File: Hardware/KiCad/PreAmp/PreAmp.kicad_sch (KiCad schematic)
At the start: 27 parts, among them J1 XLR3, J2 Conn_01x03_Pin, J3 Conn_01x05_Pin, U1 TLV2371DBV, U2 INA217AIDWR

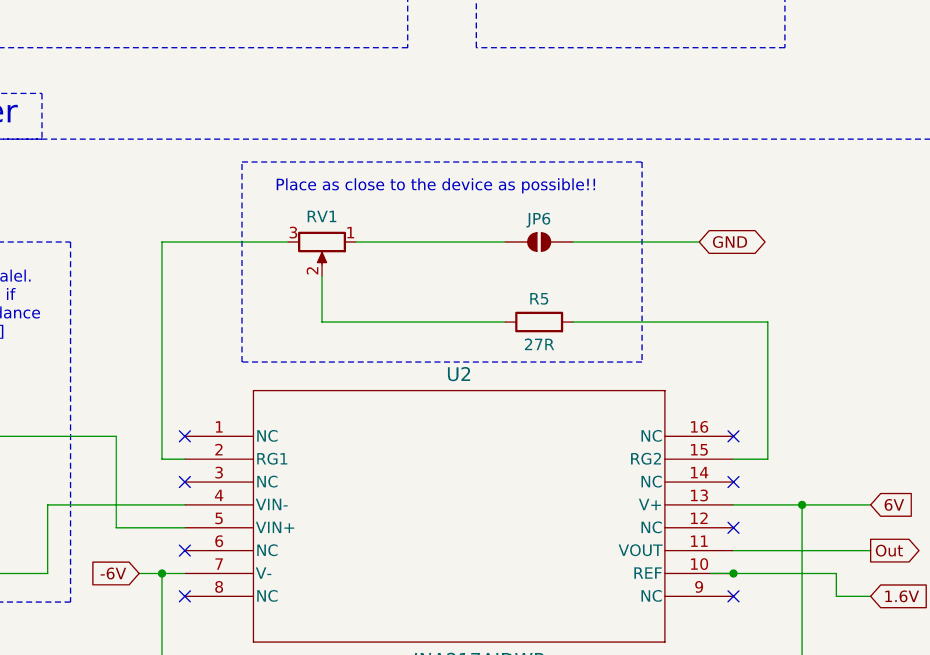
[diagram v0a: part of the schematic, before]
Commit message: Changed flow -> right to left
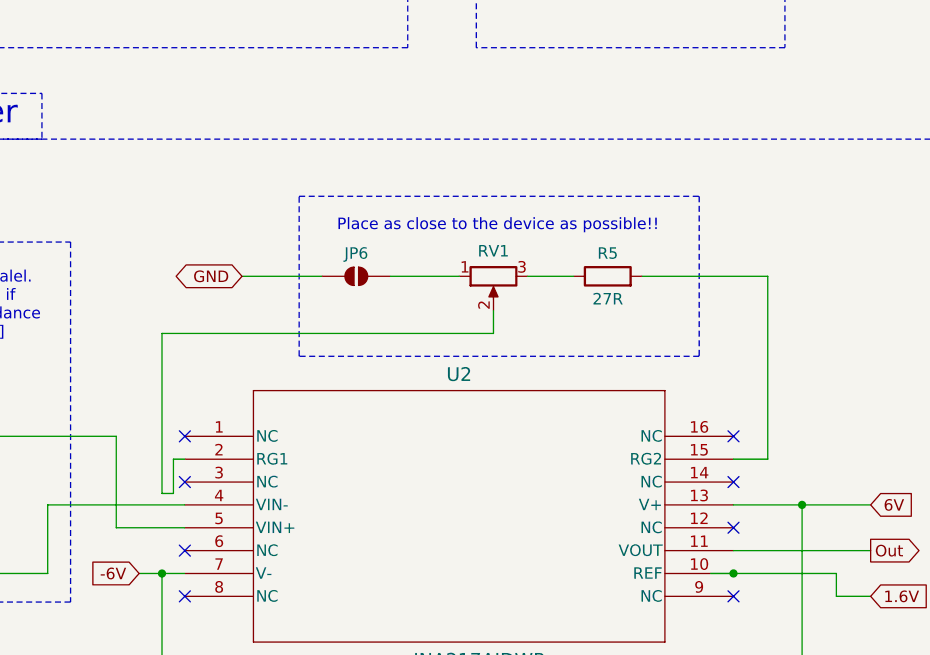
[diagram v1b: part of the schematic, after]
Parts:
- J2: footprint (none) -> Connector_PinSocket_2.54mm:PinSocket_1x03_P2.54mm_Vertical
- R1, R2, R3, R4, R5: footprint (none) -> Capacitor_SMD:C_0805_2012Metric
- TP1, TP2, TP3: footprint TestPoint:TestPoint_Pad_D3.0mm -> TestPoint:TestPoint_Pad_D2.0mm
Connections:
- net at RV1.2: now also U2.2 (RG1); no longer R5.1
- net at RV1.3: now also R5.1; no longer U2.2 (RG1)
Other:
- moved on the sheet: JP6, R5, RV1
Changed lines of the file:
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@@
 	)
 	(rectangle
-		(start 180.34 64.77)
-		(end 224.79 86.995)
+		(start 186.69 68.58)
+		(end 231.14 86.36)
 		(stroke
 			(width 0)
@@
 	(text "Place as close to the device as possible!!"
 		(exclude_from_sim no)
-		(at 201.93 67.564 0)
+		(at 208.788 71.882 0)
 		(effects
 			(font
@@
 	(wire
 		(pts
-			(xy 171.45 73.66) (xy 171.45 97.79)
-		)
-		(stroke
-			(width 0)
-			(type default)
-		)
-	)
-	(wire
-		(pts
 			(xy 170.18 41.91) (xy 163.83 41.91)
 		)
@@
 	(wire
 		(pts
-			(xy 238.76 82.55) (xy 238.76 97.79)
+			(xy 171.45 83.82) (xy 171.45 101.6)
 		)
 		(stroke
@@
 	(wire
 		(pts
+			(xy 217.17 77.47) (xy 212.09 77.47)
+		)
+		(stroke
+			(width 0)
+			(type default)
+		)
+	)
+	(wire
+		(pts
 			(xy 120.65 110.49) (xy 120.65 118.11)
 		)
@@
 	(wire
 		(pts
-			(xy 173.99 97.79) (xy 171.45 97.79)
+			(xy 171.45 83.82) (xy 208.28 83.82)
+		)
+		(stroke
+			(width 0)
+			(type default)
+		)
+	)
+	(wire
+		(pts
+			(xy 172.72 101.6) (xy 171.45 101.6)
 		)
 		(stroke
@@
 	(wire
 		(pts
-			(xy 189.23 77.47) (xy 189.23 82.55)
-		)
-		(stroke
-			(width 0)
-			(type default)
-		)
-	)
-	(wire
-		(pts
 			(xy 217.17 30.48) (xy 229.87 30.48)
 		)
@@
 	(wire
 		(pts
-			(xy 171.45 73.66) (xy 185.42 73.66)
+			(xy 172.72 97.79) (xy 173.99 97.79)
 		)
 		(stroke
@@
 	(wire
 		(pts
+			(xy 234.95 97.79) (xy 238.76 97.79)
+		)
+		(stroke
+			(width 0)
+			(type default)
+		)
+	)
+	(wire
+		(pts
 			(xy 72.39 41.91) (xy 72.39 46.99)
 		)
@@
 	(wire
 		(pts
-			(xy 118.11 45.72) (xy 124.46 45.72)
+			(xy 238.76 77.47) (xy 238.76 97.79)
 		)
 		(stroke
@@
 	(wire
 		(pts
-			(xy 234.95 97.79) (xy 238.76 97.79)
+			(xy 118.11 45.72) (xy 124.46 45.72)
 		)
 		(stroke
@@
 	(wire
 		(pts
-			(xy 217.17 82.55) (xy 238.76 82.55)
+			(xy 172.72 38.1) (xy 172.72 43.18)
 		)
 		(stroke
@@
 	(wire
 		(pts
-			(xy 172.72 38.1) (xy 172.72 43.18)
+			(xy 246.38 113.03) (xy 246.38 110.49)
 		)
 		(stroke
@@
 	(wire
 		(pts
-			(xy 246.38 113.03) (xy 246.38 110.49)
+			(xy 125.73 40.64) (xy 125.73 35.56)
 		)
 		(stroke
@@
 	(wire
 		(pts
-			(xy 125.73 40.64) (xy 125.73 35.56)
+			(xy 172.72 101.6) (xy 172.72 97.79)
 		)
 		(stroke
@@
 	(wire
 		(pts
-			(xy 193.04 73.66) (xy 209.55 73.66)
+			(xy 204.47 77.47) (xy 196.85 77.47)
 		)
 		(stroke
@@
 	(wire
 		(pts
-			(xy 189.23 82.55) (xy 209.55 82.55)
-		)
-		(stroke
-			(width 0)
-			(type default)
-		)
-	)
-	(wire
-		(pts
 			(xy 83.82 161.29) (xy 102.87 161.29)
 		)
@@
 	(wire
 		(pts
-			(xy 217.17 73.66) (xy 231.14 73.66)
+			(xy 189.23 77.47) (xy 180.34 77.47)
 		)
 		(stroke
@@
 	(wire
 		(pts
+			(xy 208.28 83.82) (xy 208.28 81.28)
+		)
+		(stroke
+			(width 0)
+			(type default)
+		)
+	)
+	(wire
+		(pts
 			(xy 90.17 80.01) (xy 106.68 80.01)
 		)
@@
 	(wire
 		(pts
+			(xy 238.76 77.47) (xy 224.79 77.47)
+		)
+		(stroke
+			(width 0)
+			(type default)
+		)
+	)
+	(wire
+		(pts
 			(xy 102.87 161.29) (xy 102.87 170.18)
 		)
@@
 	(global_label "GND"
 		(shape bidirectional)
-		(at 231.14 73.66 0)
+		(at 180.34 77.47 180)
 		(fields_autoplaced yes)
 		(effects
@@
 				(size 1.27 1.27)
 			)
-			(justify left)
+			(justify right)
 		)
 		(property "Intersheetrefs" "${INTERSHEET_REFS}"
-			(at 239.107 73.66 0)
+			(at 172.373 77.47 0)
 			(effects
 				(font
 					(size 1.27 1.27)
 				)
-				(justify left)
+				(justify right)
 				(hide yes)
 			)
@@
 			)
 		)
-		(property "Footprint" ""
+		(property "Footprint" "Capacitor_SMD:C_0805_2012Metric"
 			(at 68.072 163.83 90)
 			(effects
@@
 	(symbol
 		(lib_id "Device:R_Potentiometer")
-		(at 189.23 73.66 270)
+		(at 208.28 77.47 90)
+		(mirror x)
 		(unit 1)
 		(exclude_from_sim no)
@@
 		(dnp no)
 		(property "Reference" "RV1"
-			(at 189.23 70.866 90)
+			(at 208.28 74.676 90)
 			(effects
 				(font
@@
 		)
 		(property "Value" "R_Potentiometer"
-			(at 189.484 70.358 90)
+			(at 208.026 74.168 90)
 			(effects
 				(font
@@
 		)
 		(property "Footprint" "Potentiometer_THT:Potentiometer_Alpha_RD901F-40-00D_Single_Vertical"
-			(at 189.23 73.66 0)
+			(at 208.28 77.47 0)
 			(effects
 				(font
@@
 		)
 		(property "Datasheet" "~"
-			(at 189.23 73.66 0)
+			(at 208.28 77.47 0)
 			(effects
 				(font
@@
 		)
 		(property "Description" "Potentiometer"
-			(at 189.23 73.66 0)
+			(at 208.28 77.47 0)
 			(effects
 				(font
@@
 			)
 		)
-		(property "Footprint" ""
+		(property "Footprint" "Capacitor_SMD:C_0805_2012Metric"
 			(at 127.762 121.92 90)
 			(effects
@@
 			)
 		)
-		(property "Footprint" ""
+		(property "Footprint" "Connector_PinSocket_2.54mm:PinSocket_1x03_P2.54mm_Vertical"
 			(at 135.89 38.1 0)
 			(effects
@@
 			)
 		)
-		(property "Footprint" "TestPoint:TestPoint_Pad_D3.0mm"
+		(property "Footprint" "TestPoint:TestPoint_Pad_D2.0mm"
 			(at 115.57 170.18 0)
 			(effects
@@
 			)
 		)
-		(property "Footprint" "TestPoint:TestPoint_Pad_D3.0mm"
+		(property "Footprint" "TestPoint:TestPoint_Pad_D2.0mm"
 			(at 152.4 133.35 0)
 			(effects
@@
 			)
 		)
-		(property "Footprint" "TestPoint:TestPoint_Pad_D3.0mm"
+		(property "Footprint" "TestPoint:TestPoint_Pad_D2.0mm"
 			(at 123.19 45.72 0)
 			(effects
@@
 	(symbol
 		(lib_id "Device:R")
-		(at 213.36 82.55 90)
+		(at 220.98 77.47 90)
 		(unit 1)
 		(exclude_from_sim no)
@@
 		(dnp no)
 		(property "Reference" "R5"
-			(at 213.36 80.01 90)
+			(at 220.98 74.93 90)
 			(effects
 				(font
@@
 		)
 		(property "Value" "27R"
-			(at 213.36 85.09 90)
+			(at 220.98 80.01 90)
 			(effects
 				(font
@@
 			)
 		)
-		(property "Footprint" ""
-			(at 213.36 84.328 90)
+		(property "Footprint" "Capacitor_SMD:C_0805_2012Metric"
+			(at 220.98 79.248 90)
 			(effects
 				(font
@@
 		)
 		(property "Datasheet" "~"
-			(at 213.36 82.55 0)
+			(at 220.98 77.47 0)
 			(effects
 				(font
@@
 		)
 		(property "Description" "Resistor"
-			(at 213.36 82.55 0)
+			(at 220.98 77.47 0)
 			(effects
 				(font
@@
 			)
 		)
-		(property "Footprint" ""
+		(property "Footprint" "Capacitor_SMD:C_0805_2012Metric"
 			(at 68.072 180.34 90)
 			(effects
@@
 			)
 		)
-		(property "Footprint" ""
+		(property "Footprint" "Capacitor_SMD:C_0805_2012Metric"
 			(at 118.872 121.92 90)
 			(effects
@@
 	(symbol
 		(lib_id "Jumper:SolderJumper_2_Open")
-		(at 213.36 73.66 0)
+		(at 193.04 77.47 0)
+		(mirror y)
 		(unit 1)
 		(exclude_from_sim no)
@@
 		(dnp no)
 		(property "Reference" "JP6"
-			(at 213.36 71.12 0)
+			(at 193.04 74.93 0)
 			(effects
 				(font
@@
 		)
 		(property "Value" "SolderJumper_2_Open"
-			(at 213.36 71.12 0)
+			(at 193.04 74.93 0)
 			(effects
 				(font
@@
 		)
 		(property "Footprint" "Jumper:SolderJumper-2_P1.3mm_Open_Pad1.0x1.5mm"
-			(at 213.36 73.66 0)
+			(at 193.04 77.47 0)
 			(effects
 				(font
@@
 		)
 		(property "Datasheet" "~"
-			(at 213.36 73.66 0)
+			(at 193.04 77.47 0)
 			(effects
 				(font
@@
 		)
 		(property "Description" "Solder Jumper, 2-pole, open"
-			(at 213.36 73.66 0)
+			(at 193.04 77.47 0)
 			(effects
 				(font

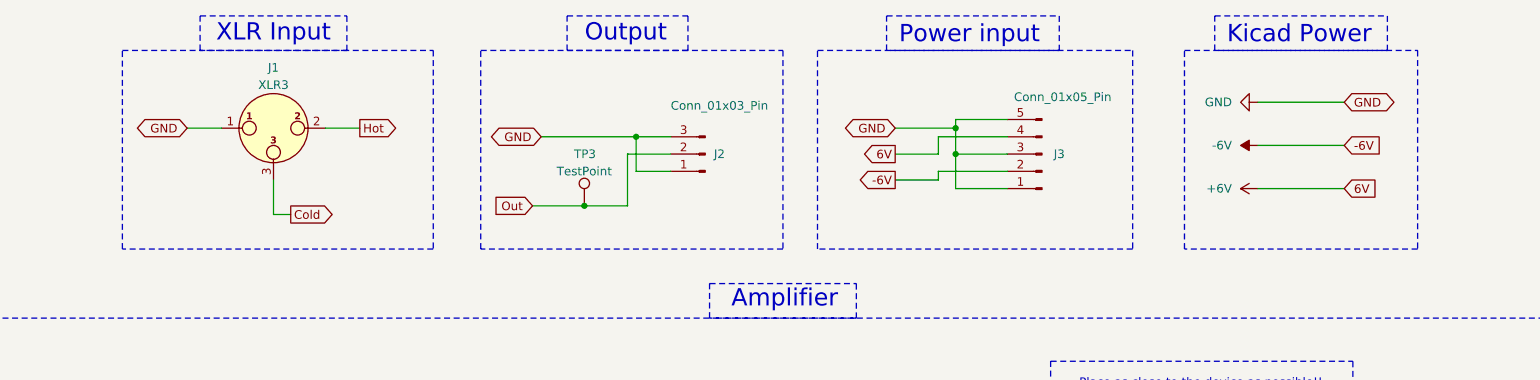
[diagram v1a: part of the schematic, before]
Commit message: Changed Header pin
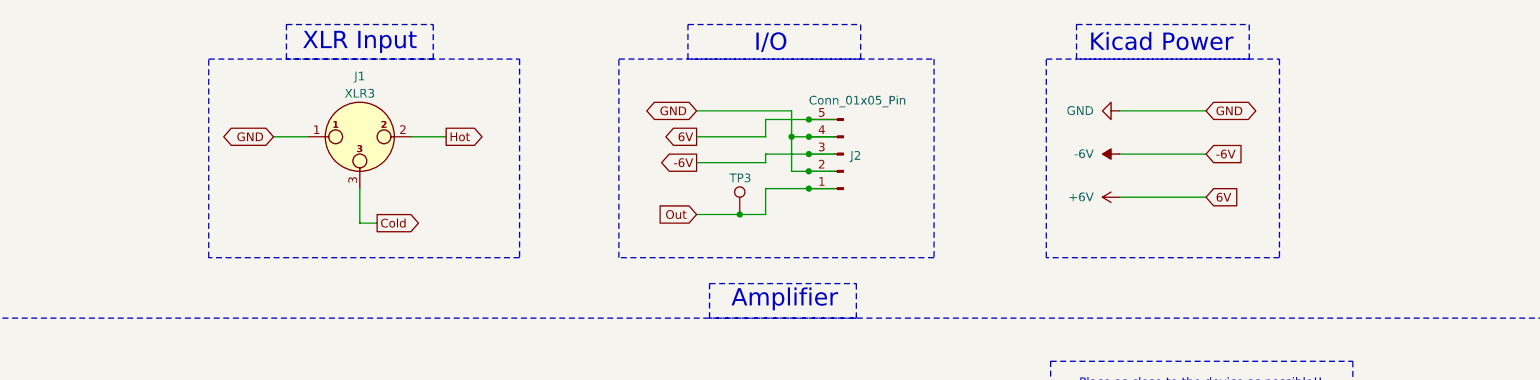
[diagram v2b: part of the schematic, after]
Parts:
- removed J2: Conn_01x03_Pin, Connector_PinSocket_2.54mm:PinSocket_1x03_P2.54mm_Vertical, symbol Connector:Conn_01x03_Pin
- removed J3: Conn_01x05_Pin, Connector_PinSocket_2.54mm:PinSocket_1x05_P2.54mm_Vertical, symbol Connector:Conn_01x05_Pin
- added J2: Conn_01x05_Pin, Connector_PinHeader_2.54mm:PinHeader_1x05_P2.54mm_Vertical, symbol Connector:Conn_01x05_Pin
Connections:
- net +6V: now also J2.5 (Pin_5)
- net -6V: now also J2.3 (Pin_3)
- net GND: now also J2.2 (Pin_2), J2.4 (Pin_4)
- net Out: now also J2.1 (Pin_1)
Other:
- note added: "I/O"
- note removed: "Output"
- note removed: "Power input"
- moved on the sheet: J1, TP3

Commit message: First part of differential routing
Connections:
- net In-: now reaches C2.2, D3.2 (A), D4.1 (K), JP4.1 (A), JP5.1 (A), R3.1
- net In+: now reaches C1.2, D1.2 (A), D2.1 (K), JP2.1 (A), JP3.1 (A), R4.1
- net Cold renamed Input-
- net Hot renamed Input+
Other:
- moved on the sheet: J1
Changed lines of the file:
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@@
 	)
 	(rectangle
-		(start 33.655 84.455)
-		(end 62.865 115.57)
+		(start 23.495 76.2)
+		(end 64.135 117.475)
 		(stroke
 			(width 0)
@@
 	)
 	(rectangle
-		(start 31.115 62.23)
+		(start 21.59 62.23)
 		(end 260.35 139.065)
 		(stroke
@@
 	(text "Keep the length of the input \nas short as possible!!!"
 		(exclude_from_sim no)
-		(at 34.29 88.646 0)
+		(at 30.988 80.772 0)
 		(effects
 			(font
@@
 	(wire
 		(pts
-			(xy 49.53 95.25) (xy 71.12 95.25)
+			(xy 52.07 95.25) (xy 71.12 95.25)
 		)
 		(stroke
@@
 	(wire
 		(pts
+			(xy 44.45 110.49) (xy 71.12 110.49)
+		)
+		(stroke
+			(width 0)
+			(type default)
+		)
+	)
+	(wire
+		(pts
 			(xy 151.13 40.64) (xy 148.59 40.64)
 		)
@@
 	(wire
 		(pts
-			(xy 72.39 35.56) (xy 77.47 35.56)
+			(xy 31.75 95.25) (xy 36.83 95.25)
 		)
 		(stroke
@@
 	(wire
 		(pts
+			(xy 44.45 110.49) (xy 44.45 102.87)
+		)
+		(stroke
+			(width 0)
+			(type default)
+		)
+	)
+	(wire
+		(pts
 			(xy 234.95 102.87) (xy 242.57 102.87)
 		)
@@
 	(wire
 		(pts
-			(xy 49.53 110.49) (xy 71.12 110.49)
+			(xy 154.94 38.1) (xy 151.13 38.1)
 		)
 		(stroke
@@
 	(wire
 		(pts
-			(xy 154.94 38.1) (xy 151.13 38.1)
+			(xy 246.38 110.49) (xy 234.95 110.49)
 		)
 		(stroke
@@
 		)
 	)
-	(wire
-		(pts
-			(xy 246.38 110.49) (xy 234.95 110.49)
+	(label "Input-"
+		(at 55.88 110.49 0)
+		(effects
+			(font
+				(size 1.27 1.27)
+			)
+			(justify left bottom)
 		)
-		(stroke
-			(width 0)
-			(type default)
+	)
+	(label "Input+"
+		(at 55.88 95.25 0)
+		(effects
+			(font
+				(size 1.27 1.27)
+			)
+			(justify left bottom)
+		)
+	)
+	(label "In-"
+		(at 85.09 110.49 0)
+		(effects
+			(font
+				(size 1.27 1.27)
+			)
+			(justify left bottom)
+		)
+	)
+	(label "In+"
+		(at 85.09 95.25 0)
+		(effects
+			(font
+				(size 1.27 1.27)
+			)
+			(justify left bottom)
 		)
 	)
@@
 		)
 	)
-	(global_label "Cold"
+	(global_label "Input-"
 		(shape output)
 		(at 87.63 48.26 0)
@@
 		)
 		(property "Intersheetrefs" "${INTERSHEET_REFS}"
-			(at 94.8484 48.26 0)
+			(at 96.9651 48.26 0)
 			(effects
 				(font
@@
 		)
 	)
-	(global_label "Hot"
-		(shape input)
-		(at 49.53 95.25 180)
-		(fields_autoplaced yes)
-		(effects
-			(font
-				(size 1.27 1.27)
-			)
-			(justify right)
-		)
-		(property "Intersheetrefs" "${INTERSHEET_REFS}"
-			(at 43.3396 95.25 0)
-			(effects
-				(font
-					(size 1.27 1.27)
-				)
-				(justify right)
-				(hide yes)
-			)
-		)
-	)
-	(global_label "Hot"
+	(global_label "Input+"
 		(shape output)
 		(at 97.79 35.56 0)
@@
 		)
 		(property "Intersheetrefs" "${INTERSHEET_REFS}"
-			(at 103.9804 35.56 0)
+			(at 107.1251 35.56 0)
 			(effects
 				(font
@@
 	(global_label "GND"
 		(shape bidirectional)
-		(at 72.39 35.56 180)
+		(at 31.75 95.25 180)
 		(fields_autoplaced yes)
 		(effects
@@
 		)
 		(property "Intersheetrefs" "${INTERSHEET_REFS}"
-			(at 64.423 35.56 0)
+			(at 23.783 95.25 0)
 			(effects
 				(font
@@
 		)
 	)
-	(global_label "Cold"
-		(shape input)
-		(at 49.53 110.49 180)
-		(fields_autoplaced yes)
-		(effects
-			(font
-				(size 1.27 1.27)
-			)
-			(justify right)
-		)
-		(property "Intersheetrefs" "${INTERSHEET_REFS}"
-			(at 42.3116 110.49 0)
-			(effects
-				(font
-					(size 1.27 1.27)
-				)
-				(justify right)
-				(hide yes)
-			)
-		)
-	)
 	(global_label "-6V"
 		(shape output)
@@
 	(symbol
 		(lib_id "Connector_Audio:XLR3")
-		(at 85.09 35.56 0)
+		(at 44.45 95.25 0)
 		(unit 1)
 		(exclude_from_sim no)
@@
 		(dnp no)
 		(property "Reference" "J1"
-			(at 85.09 26.67 0)
+			(at 44.45 86.36 0)
 			(effects
 				(font
@@
 		)
 		(property "Value" "XLR3"
-			(at 85.09 29.21 0)
+			(at 44.45 88.9 0)
 			(effects
 				(font
@@
 		)
 		(property "Footprint" "Connector_Audio:Jack_XLR_Neutrik_NC3FAAV-0_Vertical"
-			(at 85.09 35.56 0)
+			(at 44.45 95.25 0)
 			(effects
 				(font
@@
 		)
 		(property "Datasheet" "~"
-			(at 85.09 35.56 0)
+			(at 44.45 95.25 0)
 			(effects
 				(font
@@
 		)
 		(property "Description" "XLR Connector, Male or Female, 3 Pins"
-			(at 85.09 35.56 0)
+			(at 44.45 95.25 0)
 			(effects
 				(font
@@
 		)
 		(instances
-			(project ""
+			(project "PreAmp"
 				(path "/c83f892f-6017-40cb-88c0-c4e7a35464f0"
 					(reference "J1")

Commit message: Removed 4 jumper points
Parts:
- removed JP2, JP3, JP4, JP5: SolderJumper_2_Open, Jumper:SolderJumper-2_P1.3mm_Open_Pad1.0x1.5mm, symbol Jumper:SolderJumper_2_Open
- renumbered JP6 to JP1
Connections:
- net In+: now also U2.5 (VIN+)
- net In-: now also U2.4 (VIN-)
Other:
- note removed: "XLR Input"

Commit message: Put back the 4 jumpers for possible improvement (reduce oscilation)
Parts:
- added JP2, JP3, JP4, JP5: SolderJumper_2_Open, Jumper:SolderJumper-2_P1.3mm_Open_Pad1.0x1.5mm, symbol Jumper:SolderJumper_2_Open
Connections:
- net In+: now also JP2.1 (A), JP3.1 (A); no longer C1.2, D1.2 (A), D2.1 (K), R4.1
- net In-: now also JP4.1 (A), JP5.1 (A); no longer C2.2, D3.2 (A), D4.1 (K), R3.1
- net Input+ renamed XLR+
- net Input- renamed XLR-
- new net Cont+: C1.2, D1.2 (A), D2.1 (K), JP2.2 (B), JP3.2 (B), R4.1
- new net Cont-: C2.2, D3.2 (A), D4.1 (K), JP4.2 (B), JP5.2 (B), R3.1
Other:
- note added: "Optional: Extra 1.2uH + 47R paralel. This reduces oscilation if input below 10R impedance"
- note removed: "Optional: Extra 1.2uH + 47R paralel. This reduces oscilation if input below 10R impedance [NOT IN THIS VERSION]"

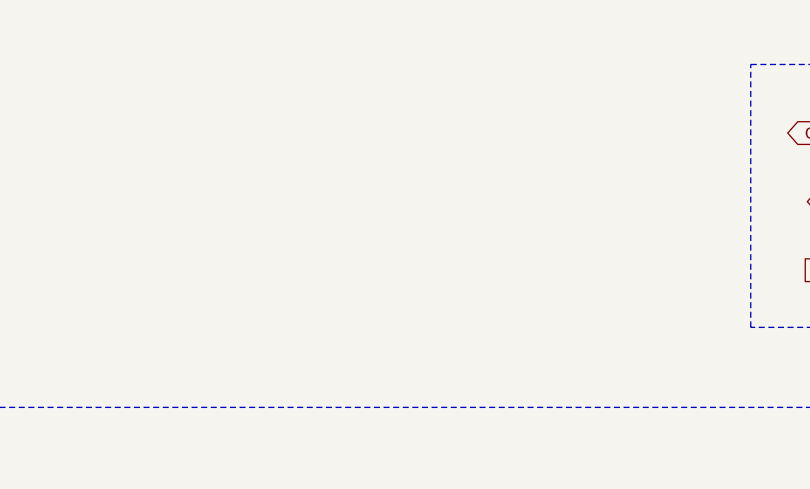
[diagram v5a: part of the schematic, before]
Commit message: Included text on PCB
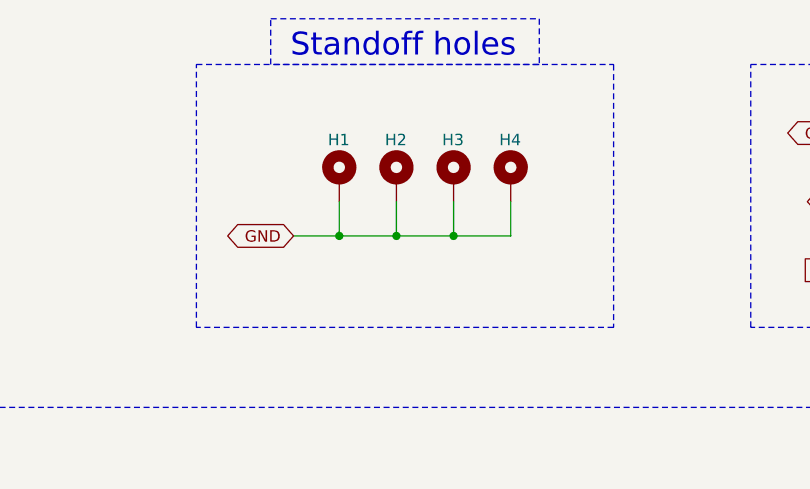
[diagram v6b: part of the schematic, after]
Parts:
- added H1, H2, H3, H4: MountingHole_Pad, MountingHole:MountingHole_3.2mm_M3_DIN965_Pad_TopBottom, symbol Mechanical:MountingHole_Pad
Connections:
- net GND: now also H1.1, H2.1, H3.1, H4.1
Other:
- note added: "Standoff holes"

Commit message: Generated files for production
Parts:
- C1, C2: footprint Capacitor_SMD:C_0805_2012Metric -> Capacitor_SMD:C_1206_3216Metric; LCSC PN (none) -> C76659
- C3, C4: footprint Capacitor_SMD:C_0805_2012Metric -> Capacitor_Tantalum_SMD:CP_EIA-3216-18_Kemet-A; LCSC PN (none) -> C7173
- D1, D2, D3, D4, J1, J2, RV1: now not fitted; now left out of the parts list
- R1: LCSC PN (none) -> C17633
- R2: LCSC PN (none) -> C2907225
- R3, R4, R5: LCSC PN (none) -> C17594
- U1: LCSC PN (none) -> C55940
- U2: LCSC PN (none) -> C1849416
